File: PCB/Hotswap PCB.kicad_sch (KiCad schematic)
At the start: 5 parts, among them J1 SSD1306_OLED, J2 JST, SW2 SW_Push, U1 Elite-C, U2 nice!nano

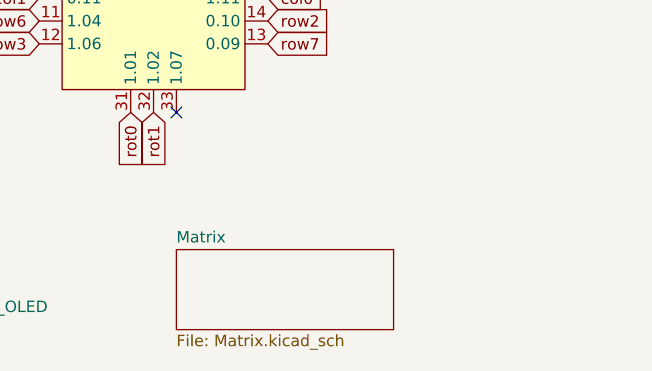
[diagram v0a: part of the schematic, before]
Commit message: Fixed a problem PCB Matrixes not being seperate. Uploaded somewhat broken ZMK firmware
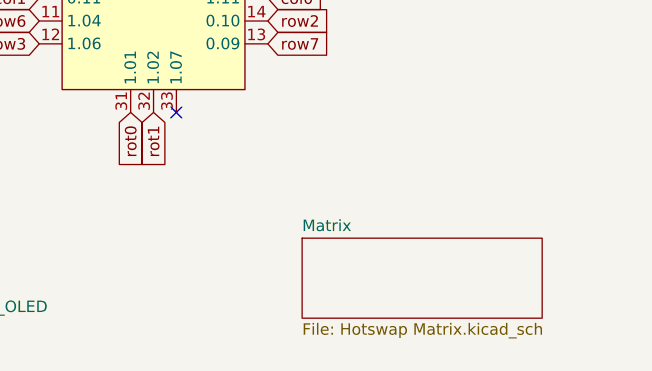
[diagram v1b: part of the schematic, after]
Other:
- sheet Matrix: file Matrix.kicad_sch -> Hotswap Matrix.kicad_sch
